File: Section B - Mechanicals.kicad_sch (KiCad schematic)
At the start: 9 parts, among them J1 Conn_02x04_Counter_Clockwise, J2 Conn_01x05_Pin

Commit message: [bugfix] fixed J1 connector footprint and power indicator D2 polarity
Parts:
- J1: footprint Connector_PinHeader_2.54mm:PinHeader_2x06_P2.54mm_Vertical -> Connector_PinHeader_2.54mm:PinHeader_2x04_P2.54mm_Vertical
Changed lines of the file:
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@@
 		(on_board yes)
 		(dnp no)
-		(fields_autoplaced yes)
 		(property "Reference" "R1"
 			(at 270.51 163.8299 0)
@@
 			)
 		)
-		(property "Footprint" "Connector_PinHeader_2.54mm:PinHeader_2x06_P2.54mm_Vertical"
+		(property "Footprint" "Connector_PinHeader_2.54mm:PinHeader_2x04_P2.54mm_Vertical"
 			(at 193.04 78.74 0)
 			(effects

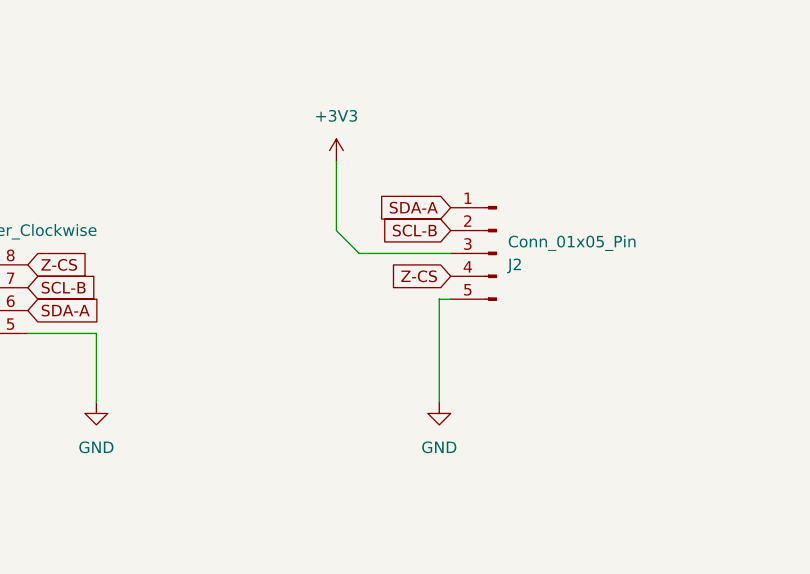
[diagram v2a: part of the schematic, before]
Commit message: fixed ERC violations
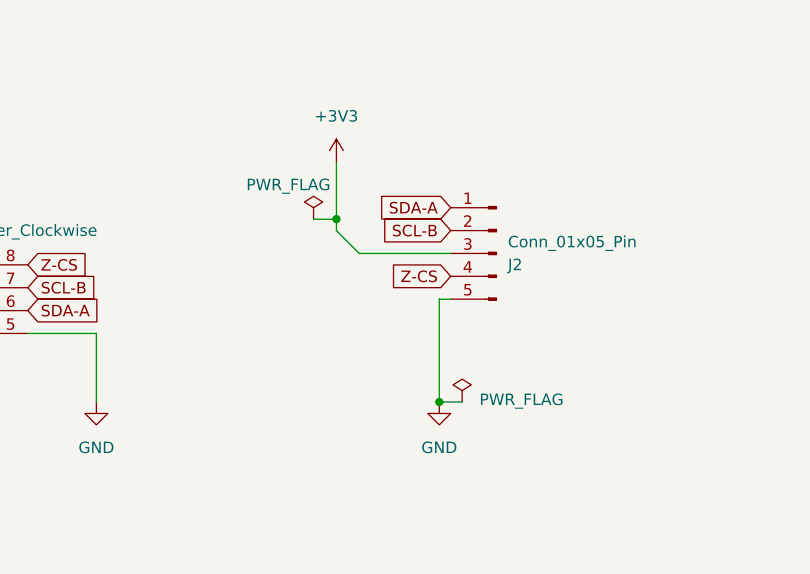
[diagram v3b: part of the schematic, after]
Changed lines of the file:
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@@
 		)
+	)
+	(junction
+		(at 234.95 71.12)
+		(diameter 0)
+		(color 0 0 0 0)
+	)
+	(junction
+		(at 246.38 91.44)
+		(diameter 0)
+		(color 0 0 0 0)
 	)
 	(wire
@@
 	(wire
 		(pts
+			(xy 234.95 71.12) (xy 234.95 72.39)
+		)
+		(stroke
+			(width 0)
+			(type default)
+		)
+	)
+	(wire
+		(pts
 			(xy 237.49 74.93) (xy 234.95 72.39)
 		)
@@
 	(wire
 		(pts
-			(xy 234.95 64.77) (xy 234.95 72.39)
+			(xy 234.95 64.77) (xy 234.95 71.12)
 		)
 		(stroke
@@
 	(wire
 		(pts
+			(xy 232.41 71.12) (xy 234.95 71.12)
+		)
+		(stroke
+			(width 0)
+			(type default)
+		)
+	)
+	(wire
+		(pts
 			(xy 200.66 83.82) (xy 208.28 83.82)
 		)
@@
 		(pts
 			(xy 173.99 74.93) (xy 173.99 81.28)
+		)
+		(stroke
+			(width 0)
+			(type default)
+		)
+	)
+	(wire
+		(pts
+			(xy 248.92 91.44) (xy 246.38 91.44)
 		)
 		(stroke
@@
 				(path "/f9e05184-c88b-4a88-ae9c-ab2bdb32be7c/c5103ceb-5325-4a84-a025-9638a412984e/e744f3ce-03a6-44a6-8792-1447ef232b9a"
 					(reference "#PWR09")
+					(unit 1)
+				)
+			)
+		)
+	)
+	(symbol
+		(lib_id "power:PWR_FLAG")
+		(at 232.41 71.12 0)
+		(unit 1)
+		(exclude_from_sim no)
+		(in_bom yes)
+		(on_board yes)
+		(dnp no)
+		(property "Reference" "#FLG01"
+			(at 232.41 69.215 0)
+			(effects
+				(font
+					(size 1.27 1.27)
+				)
+				(hide yes)
+			)
+		)
+		(property "Value" "PWR_FLAG"
+			(at 229.616 67.31 0)
+			(effects
+				(font
+					(size 1.27 1.27)
+				)
+			)
+		)
+		(property "Footprint" ""
+			(at 232.41 71.12 0)
+			(effects
+				(font
+					(size 1.27 1.27)
+				)
+				(hide yes)
+			)
+		)
+		(property "Datasheet" "~"
+			(at 232.41 71.12 0)
+			(effects
+				(font
+					(size 1.27 1.27)
+				)
+				(hide yes)
+			)
+		)
+		(property "Description" "Special symbol for telling ERC where power comes from"
+			(at 232.41 71.12 0)
+			(effects
+				(font
+					(size 1.27 1.27)
+				)
+				(hide yes)
+			)
+		)
+		(pin "1"
+		)
+		(instances
+			(project ""
+				(path "/f9e05184-c88b-4a88-ae9c-ab2bdb32be7c/c5103ceb-5325-4a84-a025-9638a412984e/e744f3ce-03a6-44a6-8792-1447ef232b9a"
+					(reference "#FLG01")
 					(unit 1)
 				)
@@
 					(unit 1)
 				)
+			)
+		)
+	)
+	(symbol
+		(lib_id "power:PWR_FLAG")
+		(at 248.92 91.44 0)
+		(unit 1)
+		(exclude_from_sim no)
+		(in_bom yes)
+		(on_board yes)
+		(dnp no)
+		(property "Reference" "#FLG02"
+			(at 248.92 89.535 0)
+			(effects
+				(font
+					(size 1.27 1.27)
+				)
+				(hide yes)
+			)
+		)
+		(property "Value" "PWR_FLAG"
+			(at 255.524 91.186 0)
+			(effects
+				(font
+					(size 1.27 1.27)
+				)
+			)
+		)
+		(property "Footprint" ""
+			(at 248.92 91.44 0)
+			(effects
+				(font
+					(size 1.27 1.27)
+				)
+				(hide yes)
+			)
+		)
+		(property "Datasheet" "~"
+			(at 248.92 91.44 0)
+			(effects
+				(font
+					(size 1.27 1.27)
+				)
+				(hide yes)
+			)
+		)
+		(property "Description" "Special symbol for telling ERC where power comes from"
+			(at 248.92 91.44 0)
+			(effects
+				(font
+					(size 1.27 1.27)
+				)
+				(hide yes)
+			)
+		)
+		(pin "1"
+		)
+		(instances
+			(project "kibot-test-cicd"
+				(path "/f9e05184-c88b-4a88-ae9c-ab2bdb32be7c/c5103ceb-5325-4a84-a025-9638a412984e/e744f3ce-03a6-44a6-8792-1447ef232b9a"
+					(reference "#FLG02")
+					(unit 1)
+				)
